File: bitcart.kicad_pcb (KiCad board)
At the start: 4 copper layers, 110 x 114.6 mm, 134 parts, among them J1 Conn_01x02, J10 Conn_01x22, J11 USB_OTG, J12 10018783-11200TLF, J13 690-008-221-904, J14 Conn_02x03_Odd_Even, J16 0455580003, J17 Molex 470531000, J2 Molex 470531000, J3 Molex 470531000, J4 Hashboard0, J5 Hashboard2, J6 Molex 470531000, J7 Hashboard1, J8 THD-20-R, J9 Hashboard3, Q1 DMP3013SFV-7, U10 PCA9546ARGVR, U13 FSUSB42MUX, U15 AP64501SP-13, U16 AP64501SP-13, U2 EMC2305-1-AP-TR, U3 MagJack-A70-112-331N126, U4 TPD4EUSB30, U5 74LVC1G07SE-7, U6 USB2514B-I/M2, U7 AP22653W6, Y1 24MHz

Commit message: added the right board outline. rotated the CM4. switched to single-shroud RA fan connectors
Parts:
- C1, C11, C14, C15, C23, C29, C3, C4, C40, C57, C58, C62, C7: value 100n -> 0.1uF
- J17, J2, J3, J6: value Molex 470531000 -> 61900411021; footprint Connector:FanPinHeader_1x04_P2.54mm_Vertical -> bitcart:CONN_61900411021_WRE
- U15: footprint CM4IO:SOIC-8-1EP_3.9x4.9mm_P1.27mm_EP2.95x4.9mm_Mask2.71x3.4mm_ThermalVias -> Package_SO:SOIC-8-1EP_3.9x4.9mm_P1.27mm_EP2.95x4.9mm_Mask2.71x3.4mm_ThermalVias
- Y1: footprint Crystal:Crystal_SMD_HC49-SD -> bitcart:CRYSTAL_ABM8G_ABR
- moved TP7 64.5 mm to (144.9, 126.2)
- moved TP8 64.5 mm to (144.9, 130.2)
- moved R35 64.2 mm to (193.8, 67.8), turned to 90 degrees
- moved R34 62.4 mm to (191.8, 67.8), turned to 90 degrees
- moved R41 61.2 mm to (193.8, 64.9), turned to 90 degrees
- moved R33 60.6 mm to (189.8, 67.8), turned to 90 degrees
- moved R40 59.2 mm to (191.8, 64.9), turned to 90 degrees
- moved R32 59.0 mm to (187.8, 67.8), turned to 90 degrees
- moved R39 57.4 mm to (189.8, 64.9), turned to 90 degrees
- moved R31 57.4 mm to (185.8, 67.8), turned to 90 degrees
- moved R38 55.6 mm to (187.8, 64.9), turned to 90 degrees
- moved R37 54.0 mm to (185.8, 64.9), turned to 90 degrees
- moved C23 50.7 mm to (151.6, 69.0), turned to 0 degrees
- moved J1 50.2 mm to (149.4, 126.9)
- moved U10 49.3 mm to (178.9, 66.1)
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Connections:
- D4 pad 1: /+12v -> Net-(D4-A)
- D4 pad 2: Net-(D4-A) -> unconnected-(D4-NC-Pad2)
- Y1 pad 2: Net-(U6-XTALOUT) -> (no net)
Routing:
- net /+3.3v: track 288.6 -> 159.4 mm, vias 24 -> 21
- net /+5v: track 196.6 -> 105.0 mm, vias 19 -> 14
- net /CM4_GPIO ( Ethernet, GPIO, SDCARD)/TRD0_P: track 67.5 -> 6.55 mm
- net /CM4_GPIO ( Ethernet, GPIO, SDCARD)/TRD0_N: track 66.8 -> 6.26 mm
- net /CM4_GPIO ( Ethernet, GPIO, SDCARD)/TRD1_N: track 69.8 -> 10.5 mm
- net /CM4_GPIO ( Ethernet, GPIO, SDCARD)/TRD1_P: track 69.0 -> 10.6 mm
- net /CM4_GPIO ( Ethernet, GPIO, SDCARD)/TRD2_N: track 65.0 -> 11.9 mm
- net /CM4_GPIO ( Ethernet, GPIO, SDCARD)/TRD2_P: track 65.6 -> 12.5 mm
- net /CM4_GPIO ( Ethernet, GPIO, SDCARD)/TRD3_N: track 64.4 -> 12.5 mm
- net /CM4_GPIO ( Ethernet, GPIO, SDCARD)/TRD3_P: track 63.8 -> 12.6 mm
- net /CM4_GPIO ( Ethernet, GPIO, SDCARD)/ETH_LEDG: track 59.3 -> 11.2 mm
- net /CM4_GPIO ( Ethernet, GPIO, SDCARD)/ETH_LEDY: track 57.2 -> 10.3 mm
- net /CM4_HighSpeed/PCIE_TX_P: track 91.7 -> 54.9 mm
- net /CM4_HighSpeed/PCIE_TX_N: track 91.6 -> 54.8 mm
- net /CM4_HighSpeed/PCIE_CLK_nREQ: track 92.6 -> 56.5 mm
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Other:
- board size 110 x 114.6 mm -> 110 x 100 mm
- board text added: "Board thickness : 1.56mm Finished copper weight inners : 1oz Finished copper weight outers : 1oz Material type : FR4 Colour of solder resists : Green Colour of silk screens : White Only on the top side 50R trace width 0.13mm@ 3GHz 90R diff pair width 0.147 spacing 0.253mm @ 2.5GHz 100R diff pair width 0.127 spacing 0.253mm @ 2GHz"
- board text removed: "Board thickness : 1.56mm Finished copper weight inners : 1oz Finished copper weight outers : 1oz Board finish : OSP Material type : FR4 Colour of solder resists : Green Colour of silk screens : White Only on the top side Board to : UL94-V0 TG >=130 50R trace width 0.13mm@ 3GHz 90R diff pair width 0.147 spacing 0.253mm @ 2.5GHz 100R diff pair width 0.127 spacing 0.253mm @ 2GHz"

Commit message: add render
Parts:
- moved J10 58.9 mm to (94.6, 114.7)
- moved R6 57.9 mm to (102.9, 118.4)
- moved R7 57.9 mm to (102.9, 119.8)
- moved C42 55.9 mm to (179.2, 114.8)
- moved D4 55.9 mm to (173.0, 115.5)
- moved C36 55.9 mm to (178.4, 121.4)
- moved C40 55.9 mm to (170.4, 115.7)
- moved Q1 55.9 mm to (177.3, 118.1)
- moved R26 55.9 mm to (172.0, 118.8)
- moved C11 53.6 mm to (151.6, 122.6)
- moved C14 53.6 mm to (142.8, 118.0)
- moved C15 53.6 mm to (147.7, 125.0)
- moved C16 53.6 mm to (164.8, 117.3)
- moved C17 53.6 mm to (134.1, 124.2)
- moved C18 53.6 mm to (151.9, 74.7)
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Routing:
- net GND: track 768.2 -> 255.9 mm, vias 233 -> 234
- net /nEXTRST: track 72.3 -> 57.1 mm
- net /CM4_HighSpeed/DSI0_D1_N: track 28.2 -> 18.9 mm, vias 2 -> 1
- net /CM4_HighSpeed/DSI0_D1_P: track 28.1 -> 19.4 mm, vias 2 -> 1
- net /+3.3v: track 159.4 -> 153.2 mm
- net /CM4_GPIO ( Ethernet, GPIO, SDCARD)/ID_SC: track 23.8 -> 22.3 mm
- net /CM4_GPIO ( Ethernet, GPIO, SDCARD)/ID_SD: track 19.2 -> 17.7 mm, vias 2 -> 1
- removed copper zone on In2.Cu, net /+3.3v
- removed copper zone on In1.Cu, net GND
- removed copper zone on In2.Cu, net GND
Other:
- outline, holes or cut-outs redrawn
- board text removed: "Ext PSU"
- board text removed: "FAN"

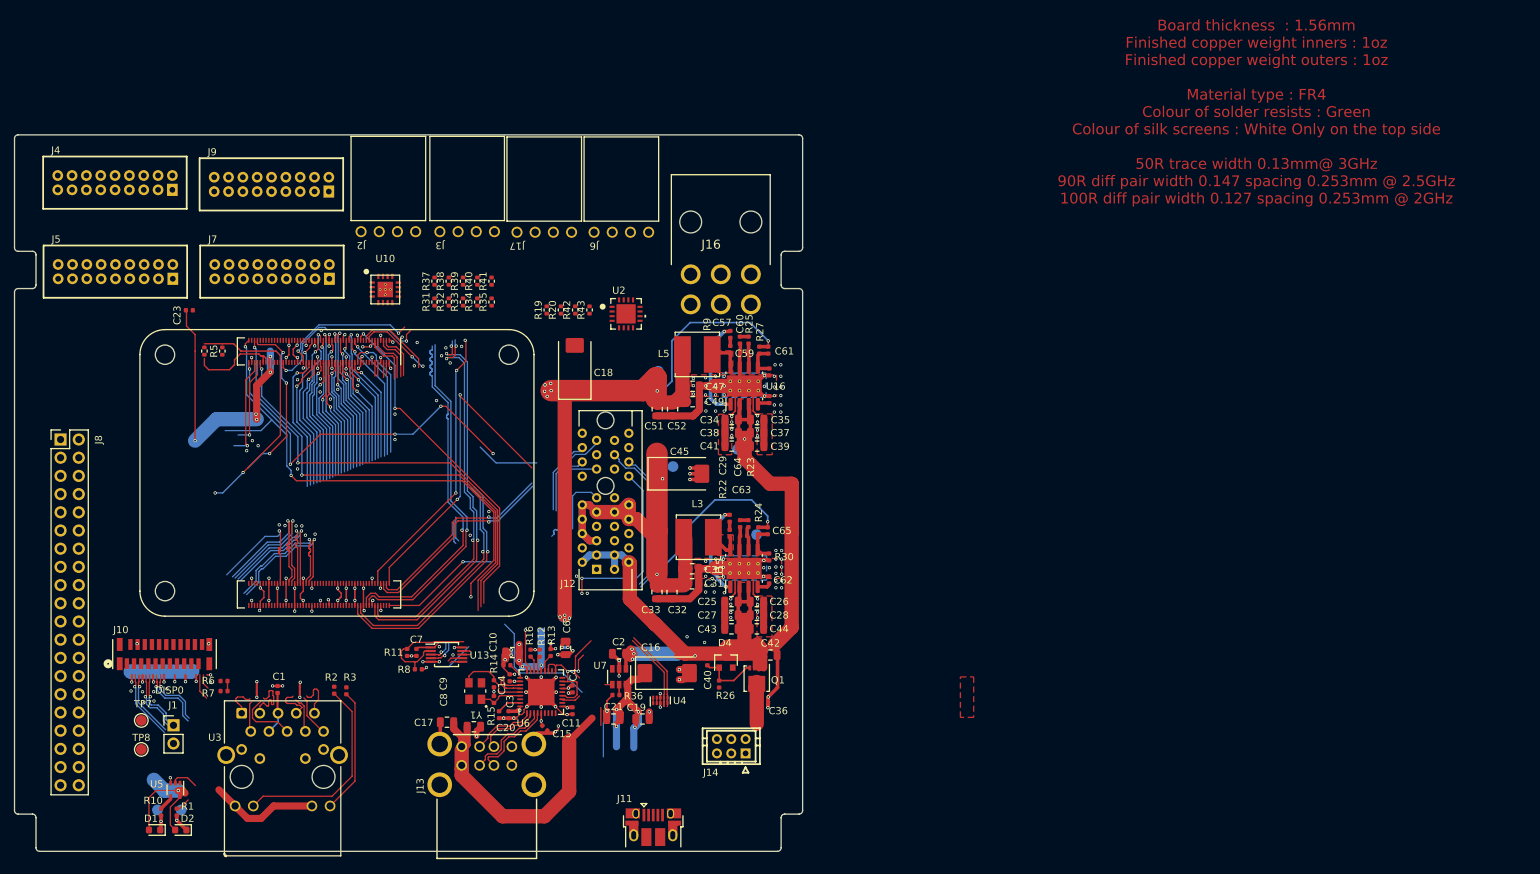
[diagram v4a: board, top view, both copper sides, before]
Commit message: resolved some schematic-board errors. switched to tap-on-top ethernet.
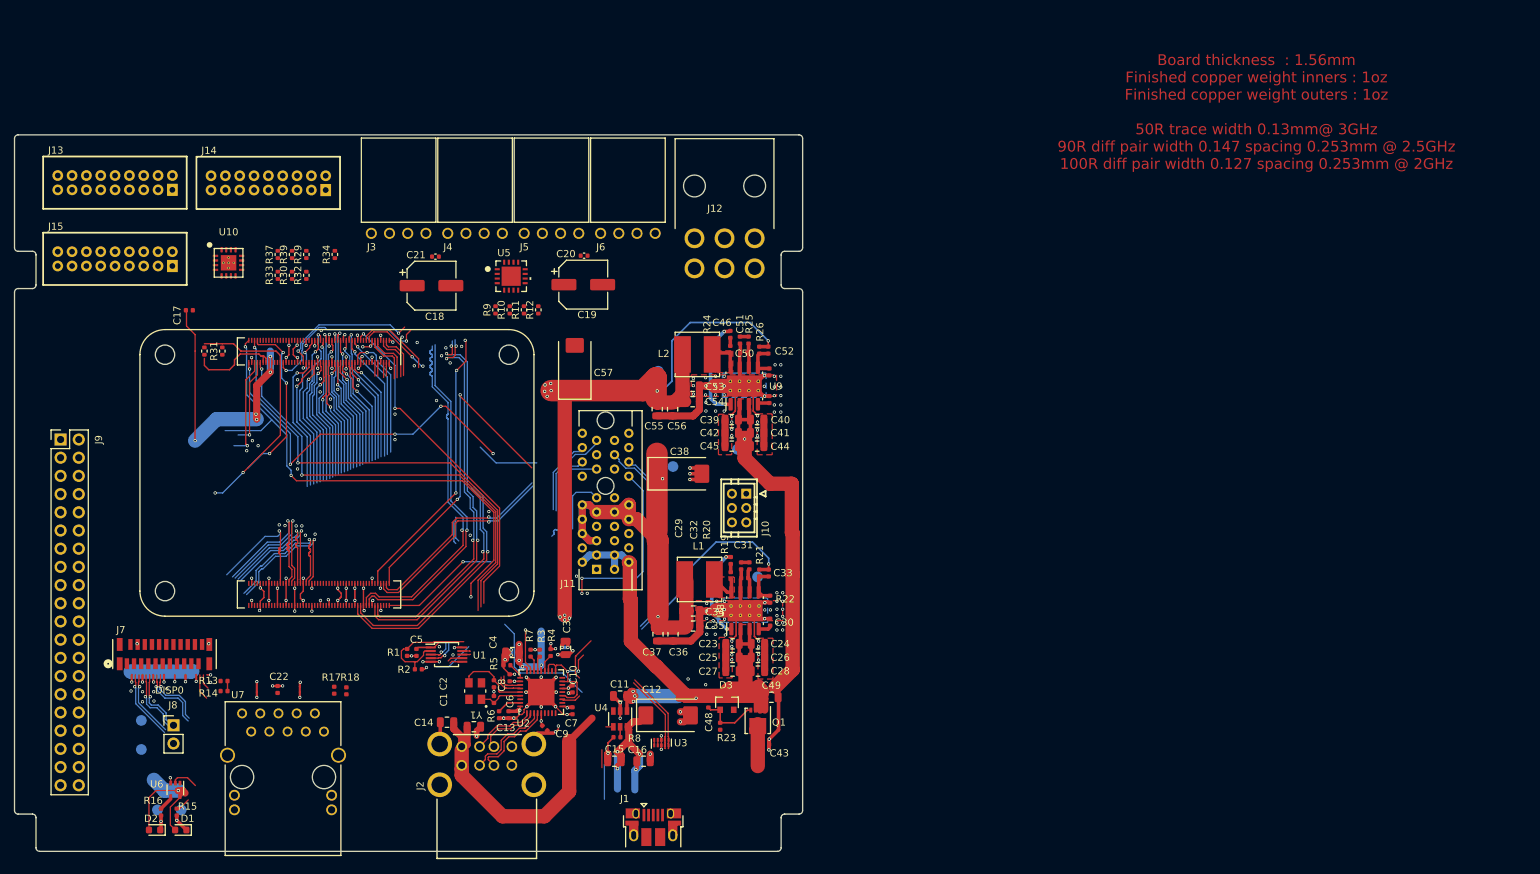
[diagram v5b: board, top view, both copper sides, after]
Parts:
- removed the J9 at (109.6, 49.1)
- removed the R34 at (138.3, 65.5)
- removed R35, R40: 4.7K, Resistor_SMD:R_0402_1005Metric
- added C18: 220uF, Capacitor_SMD:CP_Elec_6.3x7.7, F.Cu at (131.9, 63.2)
- added C19: 220uF, Capacitor_SMD:CP_Elec_6.3x7.7, F.Cu at (153.1, 63.1)
- added C20: 0.1uF, Capacitor_SMD:C_0402_1005Metric, F.Cu at (153.2, 59.1)
- added C21: 0.1uF, Capacitor_SMD:C_0402_1005Metric, F.Cu at (132.4, 59.2)
- D3: renamed from D4; footprint Diode_SMD:D_SOT-23_ANK -> bitcart:D_SOT-23_ANK
- TP1: renamed from TP7; moved to B.Cu
- TP2: renamed from TP8; moved to B.Cu
- U7: renamed from U3; footprint CM4IO:TRJG0926HENL -> bitcart:ARJM11D7-502-AB-EW2_ABR
- moved J10 33.3 mm to (174.8, 94.3), turned to 90 degrees
- moved J3 31.1 mm to (131.1, 55.9)
- moved J5 22.8 mm to (152.4, 55.9)
- moved R33 22.2 mm to (110.4, 61.8)
- moved R37 22.2 mm to (110.4, 58.9)
- moved R29 22.2 mm to (114.4, 58.9)
- moved R32 22.2 mm to (114.4, 61.8)
- moved U10 22.2 mm to (103.6, 60.1)
- moved R30 22.2 mm to (112.4, 61.8)
- moved R34 22.2 mm to (118.4, 58.9)
- moved R39 22.2 mm to (112.4, 58.9)
- moved U5 16.9 mm to (143.0, 61.9)
- moved J14 12.4 mm to (109.1, 48.9)
- moved J6 11.7 mm to (163.1, 55.9)
- moved U7 8.56 mm to (116.9, 125.5)
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- renumbered C8 to C1, C4 to C10, C2 to C11, C16 to C12, C20 to C13, C17 to C14, C21 to C15, C19 to C16, C23 to C17, C9 to C2, C1 to C22, C25 to C23, C26 to C24, C27 to C25, C28 to C26, C43 to C27, C44 to C28, C6 to C3, C62 to C30, C63 to C31, C64 to C32, C65 to C33, C30 to C34, C31 to C35, C32 to C36, C33 to C37, C45 to C38, C34 to C39, C10 to C4, C35 to C40, C37 to C41, C38 to C42, C36 to C43, C39 to C44, C41 to C45, C57 to C46, C58 to C47, C40 to C48, C42 to C49, C7 to C5, C59 to C50, C60 to C51, C61 to C52, C47 to C53, C49 to C54, C51 to C55, C52 to C56, C18 to C57, C3 to C6, C11 to C7, C14 to C8, C15 to C9, D2 to D1, D1 to D2, J11 to J1, J14 to J10, J12 to J11, J16 to J12, J4 to J13, J7 to J14, J5 to J15, J13 to J2, J6 to J3, J3 to J4, J2 to J5, J17 to J6, J10 to J7, J1 to J8, J8 to J9, L3 to L1, L5 to L2, R11 to R1, R20 to R10, R42 to R11, R43 to R12, R6 to R13, R7 to R14, R1 to R15, R10 to R16, R2 to R17, R3 to R18, R22 to R19, R8 to R2, R23 to R20, R24 to R21, R30 to R22, R26 to R23, R9 to R24, R27 to R26, R28 to R27, R4 to R28, R39 to R29, R12 to R3, R32 to R30, R5 to R31, R33 to R32, R31 to R33, R41 to R34, R38 to R39, R13 to R4, R14 to R5, R15 to R6, R16 to R7, R36 to R8, R19 to R9, TP5 to TP4, TP1 to TP5, TP2 to TP6, TP4 to TP7, TP6 to TP8, U13 to U1, U6 to U2, U4 to U3, U7 to U4, U2 to U5, U5 to U6, U15 to U8, U16 to U9
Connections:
- C22 pad 1: Net-(C1-Pad1) -> Net-(C22-Pad1)
- J4 pad 1: GND -> unconnected-(J4-Pin_1-Pad1)
- J5 pad 1: GND -> unconnected-(J5-Pin_1-Pad1)
- J7 pad 23: (no net) -> GND
- J7 pad 24: (no net) -> GND
- J7 pad 25: (no net) -> GND
- J7 pad 26: (no net) -> GND
- R13 pad 1: /+3.3v -> /CM4_GPIO ( Ethernet, GPIO, SDCARD)/+3.3v
- R14 pad 1: /+3.3v -> /CM4_GPIO ( Ethernet, GPIO, SDCARD)/+3.3v
- R17 pad 1: Net-(U3-LEDG_K) -> Net-(U7-LEDG_K)
- R18 pad 1: Net-(U3-LEDY_K) -> Net-(U7-LEDY_K)
- U10 pad 10: /hashboards/SCL3 -> unconnected-(U10-SC3-Pad10)
- U10 pad 9: /hashboards/SDA3 -> unconnected-(U10-SD3-Pad9)
- U6 pad 1: (no net) -> unconnected-(U6-Pad1)
- U7 pad 11: /CM4_GPIO ( Ethernet, GPIO, SDCARD)/TR0_TAP -> /+3.3v
- U7 pad 12: /CM4_GPIO ( Ethernet, GPIO, SDCARD)/TR1_TAP -> Net-(U7-LEDG_K)
- U7 pad 13: /CM4_GPIO ( Ethernet, GPIO, SDCARD)/TR2_TAP -> /+3.3v
- U7 pad 14: /CM4_GPIO ( Ethernet, GPIO, SDCARD)/TR3_TAP -> Net-(U7-LEDY_K)
- U7 pad 15: /+3.3v -> GND
- U7 pad 16: Net-(U3-LEDG_K) -> GND
- U7 pad 4: Net-(C1-Pad1) -> /CM4_GPIO ( Ethernet, GPIO, SDCARD)/TRD1_N
- U7 pad 5: Net-(C1-Pad1) -> Net-(C22-Pad1)
- U7 pad 6: /CM4_GPIO ( Ethernet, GPIO, SDCARD)/TRD1_N -> Net-(C22-Pad1)
- Y1 pad 2: (no net) -> unconnected-(Y1-Pad2)
- Y1 pad 4: (no net) -> unconnected-(Y1-Pad4)
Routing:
- net Net-(U3-LEDG_K): track 28.1 -> 0.00 mm
- net Net-(J1-VBUS): track 23.1 -> 0.75 mm
- net (no net): track 0.00 -> 22.3 mm
- net Net-(U3-LEDY_K): track 17.5 -> 0.00 mm
- net /+3.3v: track 153.2 -> 136.4 mm
- net /+12v: track 120.6 -> 132.5 mm
- net /CM4_GPIO ( Ethernet, GPIO, SDCARD)/TRD1_P: track 10.6 -> 1.95 mm
- net /CM4_GPIO ( Ethernet, GPIO, SDCARD)/TRD1_N: track 10.5 -> 2.10 mm
- net /CM4_GPIO ( Ethernet, GPIO, SDCARD)/TRD3_P: track 12.6 -> 6.56 mm
- net Net-(C1-Pad1): track 5.83 -> 0.00 mm
- net /CM4_GPIO ( Ethernet, GPIO, SDCARD)/TRD3_N: track 12.5 -> 6.72 mm
- net /CM4_GPIO ( Ethernet, GPIO, SDCARD)/TRD2_P: track 12.5 -> 7.20 mm
- net /CM4_GPIO ( Ethernet, GPIO, SDCARD)/TRD2_N: track 11.9 -> 7.05 mm
- net /PCIe-connector/+3.3v: track 91.1 -> 95.9 mm
- net /CM4_GPIO ( Ethernet, GPIO, SDCARD)/TRD0_P: track 6.55 -> 1.91 mm
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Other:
- board text added: "Board thickness : 1.56mm Finished copper weight inners : 1oz Finished copper weight outers : 1oz 50R trace width 0.13mm@ 3GHz 90R diff pair width 0.147 spacing 0.253mm @ 2.5GHz 100R diff pair width 0.127 spacing 0.253mm @ 2GHz"
- board text removed: "Board thickness : 1.56mm Finished copper weight inners : 1oz Finished copper weight outers : 1oz Material type : FR4 Colour of solder resists : Green Colour of silk screens : White Only on the top side 50R trace width 0.13mm@ 3GHz 90R diff pair width 0.147 spacing 0.253mm @ 2.5GHz 100R diff pair width 0.127 spacing 0.253mm @ 2GHz"
